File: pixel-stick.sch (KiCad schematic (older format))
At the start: 18 parts, among them J1 WS281*, J2 ISP, Q1 BSS138, SW1 RESET, SW2 PROG, U1 LM3670MF, U2 RT9361A, U4 ESP-M2

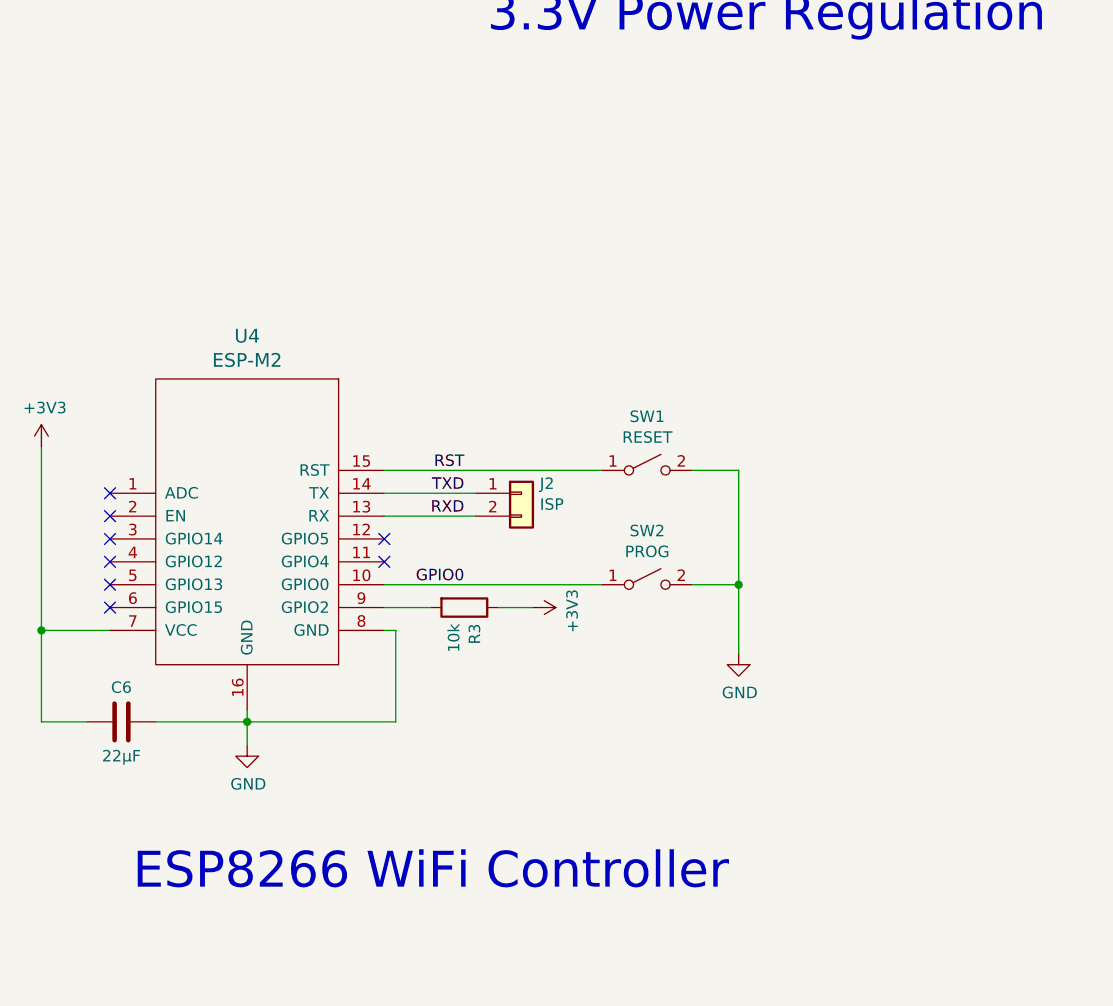
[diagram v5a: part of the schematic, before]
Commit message: make design work for ESP-01 or ESP-M2
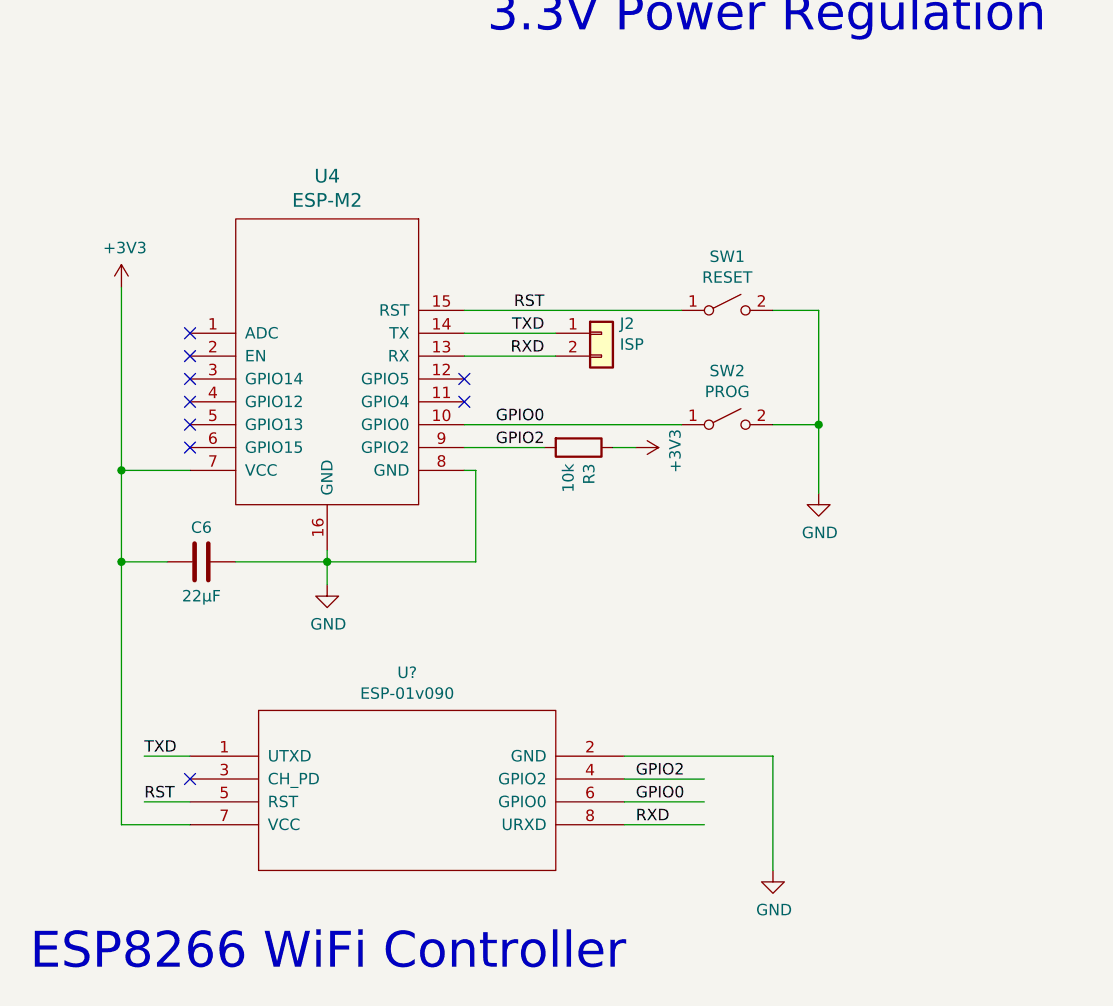
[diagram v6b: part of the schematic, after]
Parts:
- added U?: ESP-01v090, symbol ESP8266:ESP-01v090
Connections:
- net labels added: GPIO2
- wire segments 74 -> 83
- no-connect marks 8 -> 9
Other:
- moved on the sheet: C6, J2, R3, SW1, SW2, U4

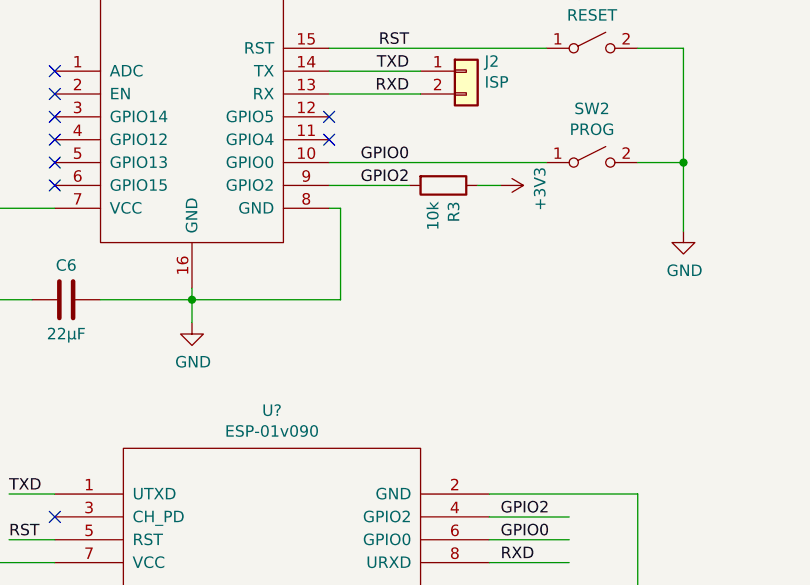
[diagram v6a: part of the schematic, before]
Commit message: remove resistor from GPIO2 pull-up
may have been a bad idea ... will need to check that things still work. Its possible the ESP-01 and ESP-M2 have internal pull ups alredy enabled and I can remove the external 3V3 entirely.
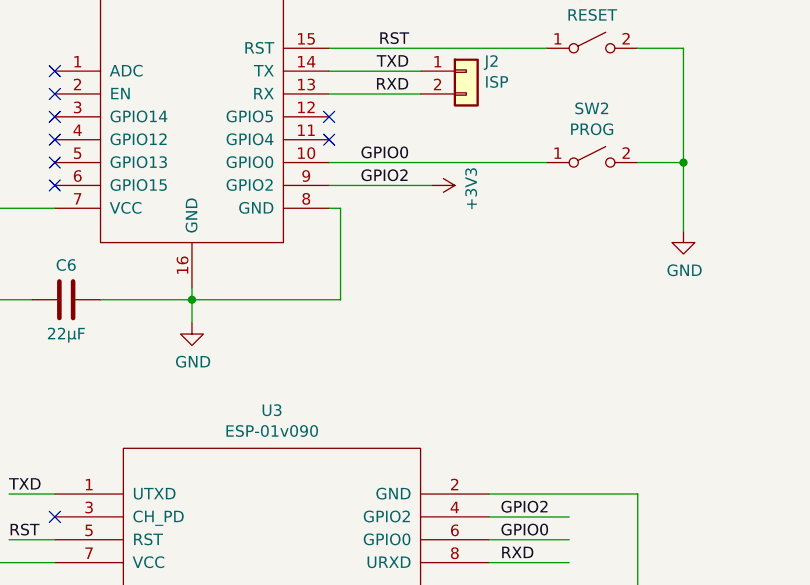
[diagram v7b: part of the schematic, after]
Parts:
- removed R3: 10k, Resistor_SMD:R_0805_2012Metric, symbol Device:R
- U3: renamed from U?; footprint (none) -> ESP8266:ESP-01
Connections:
- wire segments 83 -> 82
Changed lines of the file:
@@
 L power:+3V3 #PWR0115
 U 1 1 5E01631B
-P 3850 4650
-F 0 "#PWR0115" H 3850 4500 50  0001 C CNN
-F 1 "+3V3" H 3865 4823 50  0000 C CNN
-F 2 "" H 3850 4650 50  0001 C CNN
-F 3 "" H 3850 4650 50  0001 C CNN
-	1    3850 4650
+P 3550 4650
+F 0 "#PWR0115" H 3550 4500 50  0001 C CNN
+F 1 "+3V3" H 3565 4823 50  0000 C CNN
+F 2 "" H 3550 4650 50  0001 C CNN
+F 3 "" H 3550 4650 50  0001 C CNN
+	1    3550 4650
 	0    1    1    0
 $EndComp
@@
 	4650 4550 4650 4850
 Wire Wire Line
-	3100 4650 3450 4650
-Wire Wire Line
-	3750 4650 3850 4650
-$Comp
-L Device:R R3
-U 1 1 5E07A1B1
-P 3600 4650
-F 0 "R3" H 3670 4696 50  0000 L CNN
-F 1 "10k" H 3670 4605 50  0000 L CNN
-F 2 "Resistor_SMD:R_0805_2012Metric" V 3530 4650 50  0001 C CNN
-F 3 "~" H 3600 4650 50  0001 C CNN
-	1    3600 4650
-	0    1    1    0
-$EndComp
-Wire Wire Line
 	2500 5150 2100 5150
 Wire Wire Line
@@
 Connection ~ 1600 4750
 $Comp
-L ESP8266:ESP-01v090 U?
+L ESP8266:ESP-01v090 U3
 U 1 1 5DFAF42D
 P 2850 6150
-F 0 "U?" H 2850 6665 50  0000 C CNN
+F 0 "U3" H 2850 6665 50  0000 C CNN
 F 1 "ESP-01v090" H 2850 6574 50  0000 C CNN
-F 2 "" H 2850 6150 50  0001 C CNN
+F 2 "ESP8266:ESP-01" H 2850 6150 50  0001 C CNN
 F 3 "http://l0l.org.uk/2014/12/esp8266-modules-hardware-guide-gotta-catch-em-all/" H 2850 6150 50  0001 C CNN
 	1    2850 6150
@@
 RST
 $Comp
-L power:GND #PWR?
+L power:GND #PWR0111
 U 1 1 5DFBBB8E
 P 4450 6500
-F 0 "#PWR?" H 4450 6250 50  0001 C CNN
+F 0 "#PWR0111" H 4450 6250 50  0001 C CNN
 F 1 "GND" H 4455 6327 50  0000 C CNN
 F 2 "" H 4450 6500 50  0001 C CNN
@@
 Text Label 3850 6300 0    50   ~ 0
 RXD
+Wire Wire Line
+	3100 4650 3550 4650
 $EndSCHEMATC

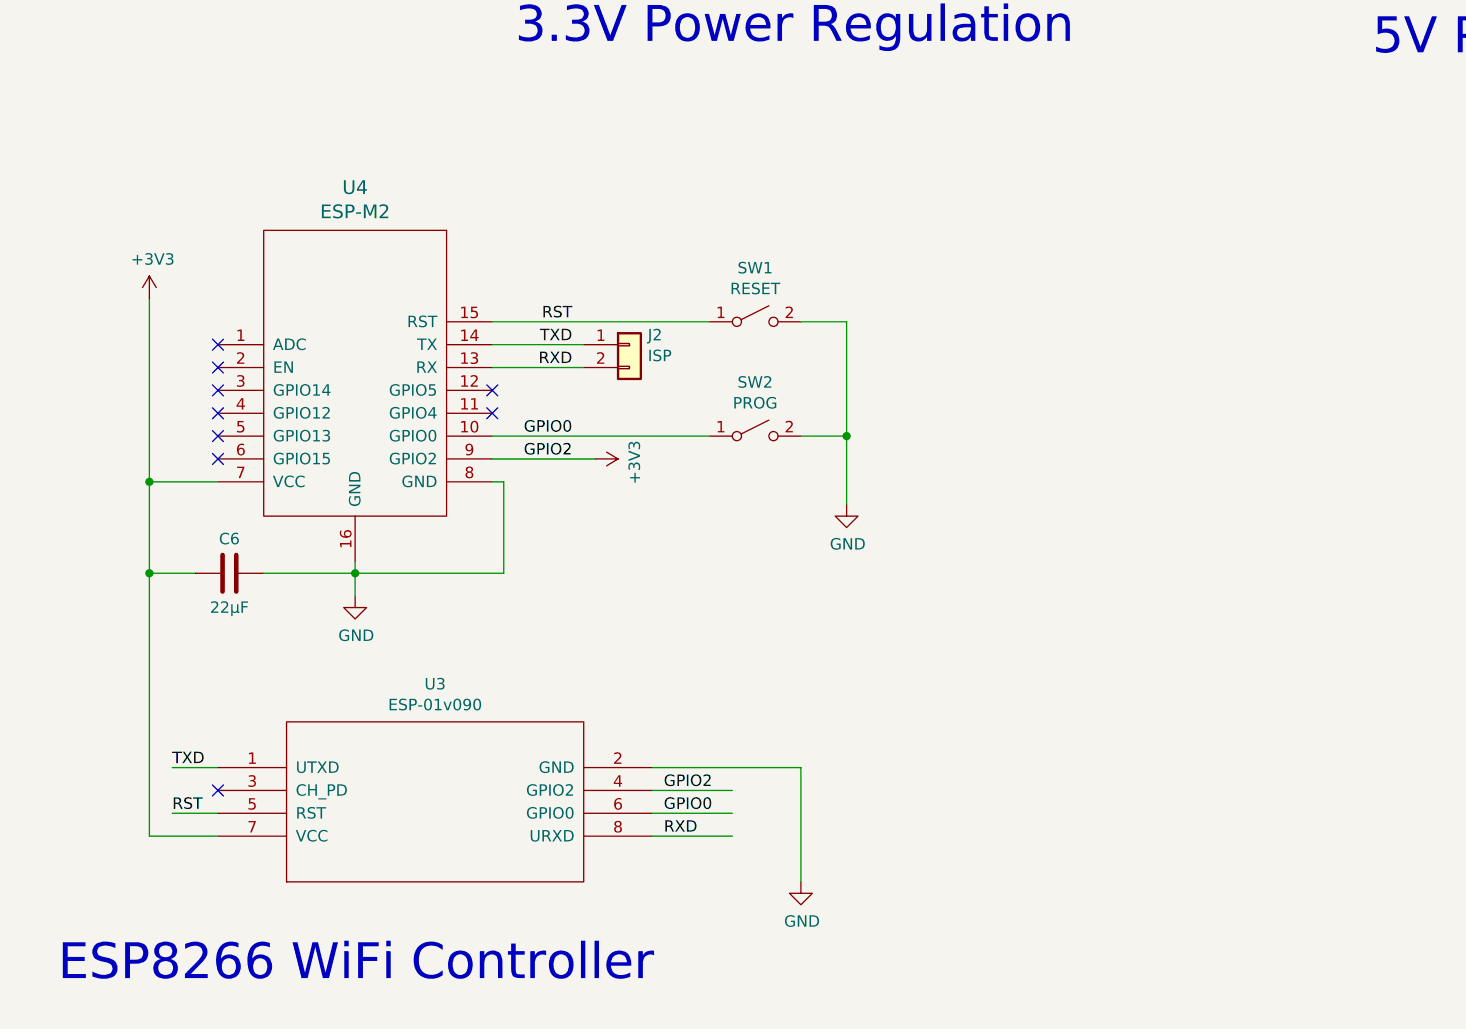
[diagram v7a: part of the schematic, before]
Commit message: Add R3 back to GPIO2
Also re-laid out the microcontrollers in schematic to make it clearer how the common interface is achieved.
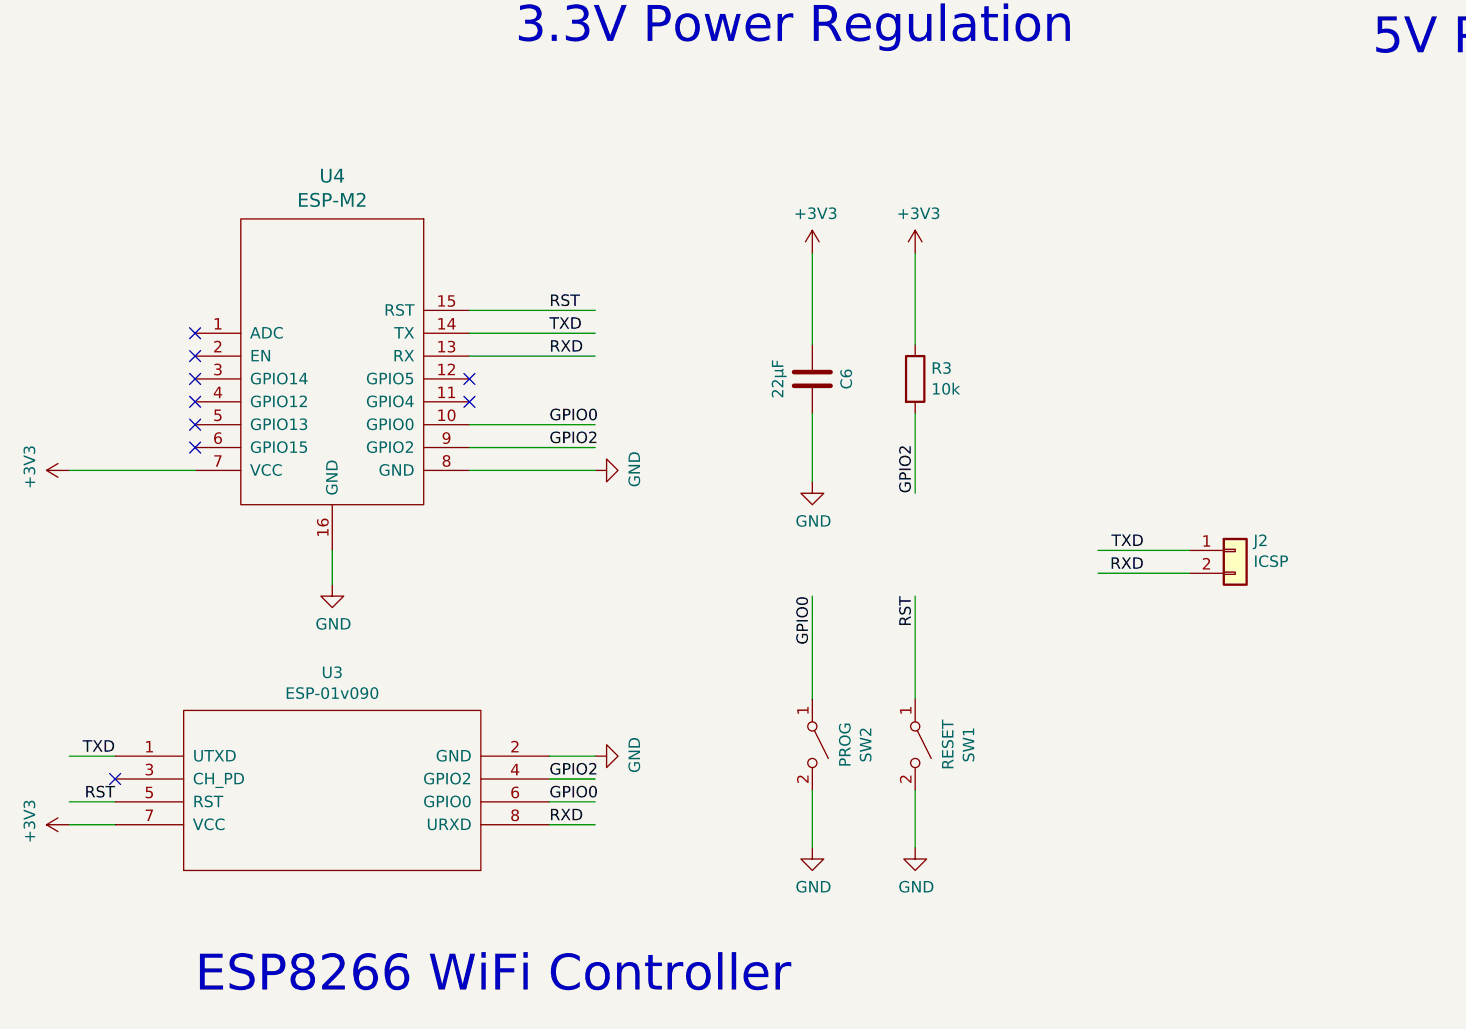
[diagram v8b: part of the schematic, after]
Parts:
- added R3: 10k, Resistor_SMD:R_0805_2012Metric, symbol Device:R
- J2: value ISP -> ICSP
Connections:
- wire segments 82 -> 79
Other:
- moved on the sheet: C6, J2, SW1, SW2, U3, U4
